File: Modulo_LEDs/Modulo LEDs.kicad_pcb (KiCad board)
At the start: 2 copper layers, 33 x 61.6 mm, 18 parts, among them J1 Conn_01x09_Female, J2 Conn_01x09_Male

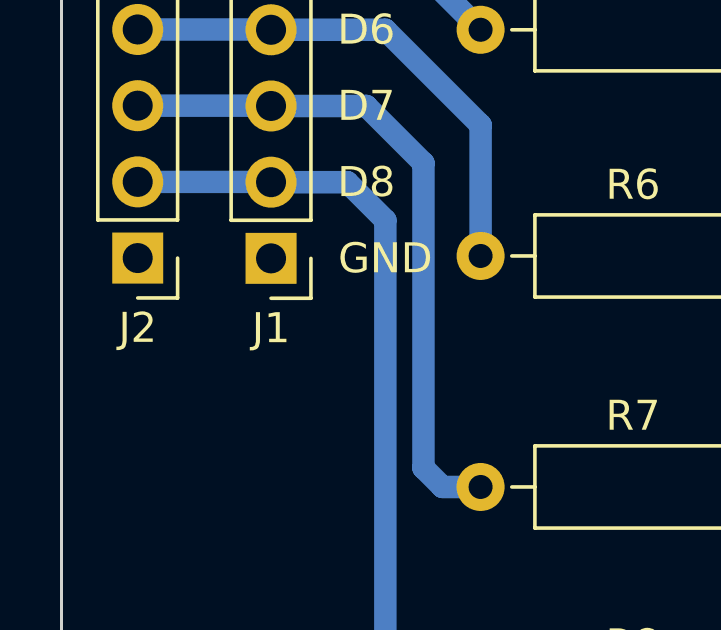
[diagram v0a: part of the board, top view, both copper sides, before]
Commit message: Arreglado path de las carpetas, agregado el README.md y los archivos para la impresion
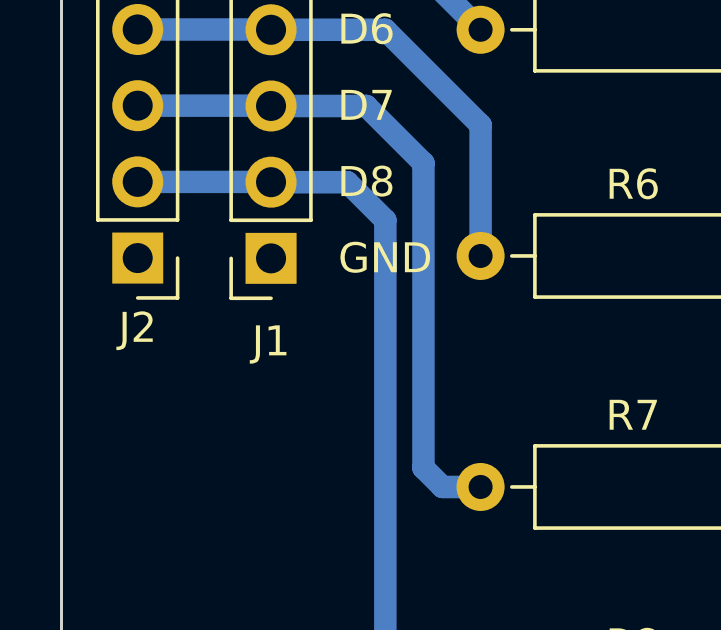
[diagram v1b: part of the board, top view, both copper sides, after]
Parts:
- J1: footprint Connector_PinHeader_2.54mm:PinHeader_1x09_P2.54mm_Vertical -> Connector_PinSocket_2.54mm:PinSocket_1x09_P2.54mm_Vertical

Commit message: Fixed PCb
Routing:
- net Net-(D6-Pad2): track 0.11 -> 5.23 mm
- net Net-(D8-Pad2): track 0.00 -> 5.08 mm
- net Net-(D2-Pad2): track 0.00 -> 5.08 mm
- net Net-(D1-Pad2): track 0.00 -> 5.08 mm
- net Net-(D7-Pad2): track 0.00 -> 5.08 mm
- net Net-(D5-Pad2): track 0.00 -> 5.08 mm
- net Net-(D4-Pad2): track 0.00 -> 5.08 mm
- net Net-(D3-Pad2): track 0.00 -> 5.08 mm
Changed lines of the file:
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@@
     (style (thickness 0.15) (arrow_length 1.27) (text_position_mode 0) (extension_height 0.58642) (extension_offset 0.5) keep_text_aligned)
   )
+  (segment (start 86.36 81.28) (end 91.435 81.28) (width 1) (layer "B.Cu") (net 1))
+  (segment (start 91.435 81.28) (end 91.44 81.285) (width 1) (layer "B.Cu") (net 1))
+  (segment (start 86.36 88.9) (end 91.435 88.9) (width 1) (layer "B.Cu") (net 2))
+  (segment (start 91.435 88.9) (end 91.44 88.905) (width 1) (layer "B.Cu") (net 2))
+  (segment (start 86.36 96.52) (end 91.44 96.52) (width 1) (layer "B.Cu") (net 3))
+  (segment (start 86.36 104.14) (end 91.44 104.14) (width 1) (layer "B.Cu") (net 4))
+  (segment (start 86.36 111.76) (end 91.44 111.76) (width 1) (layer "B.Cu") (net 5))
+  (segment (start 91.36 119.3) (end 91.44 119.38) (width 1) (layer "B.Cu") (net 6))
   (segment (start 90.725 119.3) (end 90.805 119.38) (width 0.75) (layer "B.Cu") (net 6))
+  (segment (start 86.36 119.3) (end 91.36 119.3) (width 1) (layer "B.Cu") (net 6))
+  (segment (start 86.36 127) (end 91.44 127) (width 1) (layer "B.Cu") (net 7))
+  (segment (start 86.36 134.62) (end 91.435 134.62) (width 1) (layer "B.Cu") (net 8))
+  (segment (start 91.435 134.62) (end 91.44 134.625) (width 1) (layer "B.Cu") (net 8))
   (segment (start 71.755 116.84) (end 73.025 118.11) (width 0.75) (layer "B.Cu") (net 10))
   (segment (start 73.025 133.35) (end 74.295 134.62) (width 0.75) (layer "B.Cu") (net 10))
@@
     (polygon
       (pts
-        (xy 95.25 139.7)
-        (xy 62.23 139.7)
-        (xy 62.23 78.105)
-        (xy 95.25 78.105)
+        (xy 97.79 143.51)
+        (xy 59.69 143.51)
+        (xy 59.69 74.93)
+        (xy 97.79 74.93)
       )
     )
